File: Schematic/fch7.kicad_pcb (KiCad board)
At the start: 4 copper layers, 39.8 x 41.5 mm, 145 parts, among them IC1 MP9943AGQ-Z, IC2 MP9943AGQ-Z, IC3 STM32H743VIT6, IC4 ICM-42688-P, IC5 MPU-6500, J11 PIN2216, J12 PIN2216, J2 PIN2216, J3 PIN2216, J4 PIN2216, J5 PIN2216, J6 PIN2216, J7 PIN2216, J8 PIN2216, J9 PIN2216, U1 ME6217C33M5G, U10 HDGC1002WR-S-4P, U11 HDGC1002WR-S-4P, U12 E28-2G4M27SX, U15 HDGC1002WR-S-6P, U16 HDGC1002WR-S-8P, U17 HDGC1002WR-S-8P, U2 ME6217C33M5G, U3 LDO-1.8v, U4 QMC5883L, U5 SPL06-001, U6 CSNP1GCR01-BOW, U7 HDGC1002WR-S-6P, U8 HDGC1002WR-S-4P, U9 HDGC1002WR-S-4P, Y1 8MHz

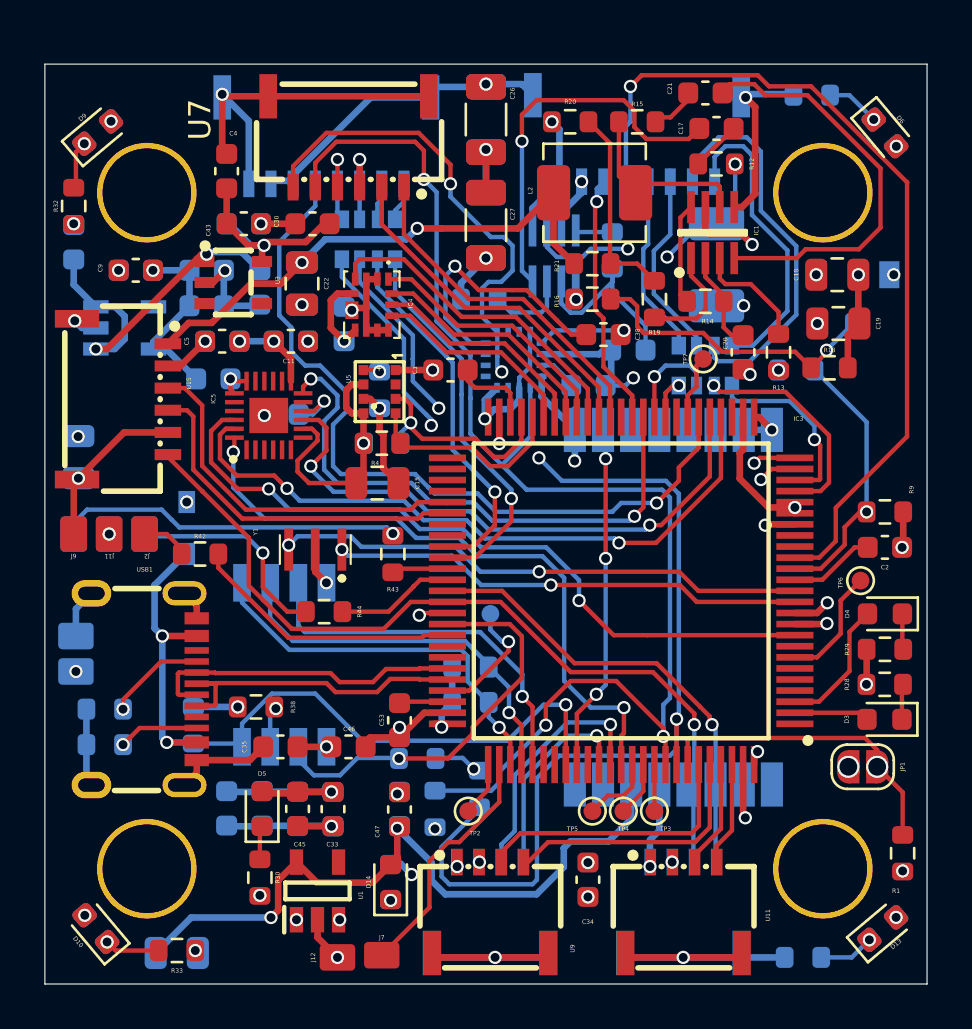
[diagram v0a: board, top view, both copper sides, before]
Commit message: switched mcu package to use TFBGA-100 8x8mm (stm32h743vih6)
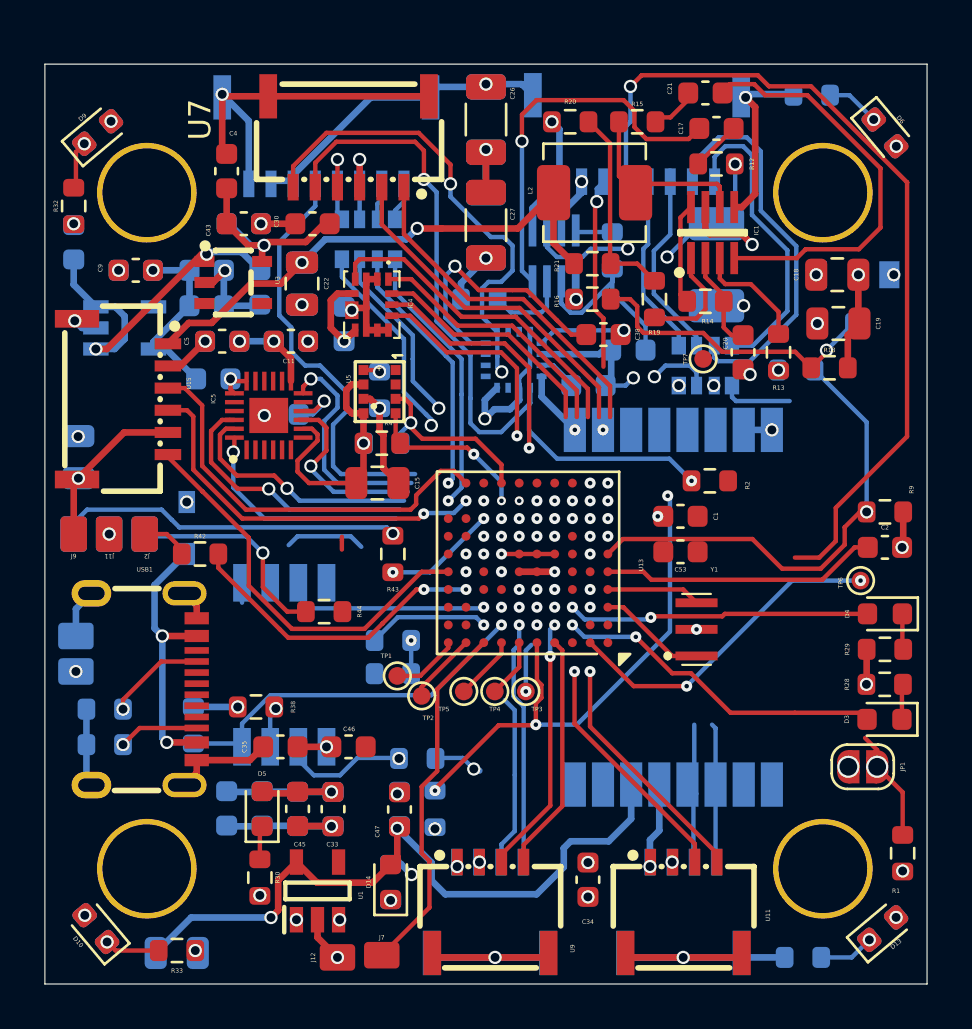
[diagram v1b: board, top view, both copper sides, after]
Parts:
- removed IC3: STM32H743VIT6, fch7:LQFP-100_14x14mm_P0.5mm_STM32H743
- added U13: STM32H742VIHx, Package_BGA:TFBGA-100_8x8mm_Layout10x10_P0.8mm, F.Cu at (86.2, 82.7)
- R2, TP1: moved to F.Cu
- moved Y1 17.6 mm to (93.8, 85.7), turned to -90 degrees
- moved R2 17.4 mm to (94.4, 79.0), turned to 180 degrees
- moved C53 14.8 mm to (93.1, 82.2), turned to 0 degrees
- moved C1 12.3 mm to (93.1, 80.6), turned to 0 degrees
- moved TP3 7.92 mm to (86.1, 88.5)
- moved TP4 7.92 mm to (84.7, 88.5)
- moved TP5 7.92 mm to (83.3, 88.5)
- moved TP2 5.61 mm to (81.4, 88.7)
- moved TP1 5.05 mm to (80.3, 87.8), turned to 0 degrees
- moved R35 3.73 mm to (80.1, 87.7), turned to 0 degrees
- moved R36 3.70 mm to (80.1, 86.2), turned to 0 degrees
- turned C2 to 180 degrees
- turned R4 to 180 degrees
- turned R5 to 180 degrees
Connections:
- C2 pad 1: /MCU/NRST -> GND
- C2 pad 2: GND -> /MCU/NRST
- R2 pad 2: I2C1_SDA -> I2C1_SCL
- R3 pad 2: I2C1_SCL -> I2C1_SDA
- R4 pad 1: VDD_MCU -> I2C2_SCL
- R4 pad 2: I2C2_SCL -> VDD_MCU
- R5 pad 1: VDD_MCU -> I2C2_SDA
- R5 pad 2: I2C2_SDA -> VDD_MCU
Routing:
- net I2C1_SCL: track 61.4 -> 33.3 mm
- net SPI1_IMU1_CS: track 32.8 -> 12.1 mm, vias 2 -> 1
- net SPI1_MOSI: track 29.4 -> 10.2 mm
- net SPI1_SCLK: track 30.0 -> 10.9 mm
- net SPI1_MISO: track 26.4 -> 8.35 mm
- net GND: track 151.8 -> 134.3 mm, vias 44 -> 42
- net SDIO_D2: track 17.8 -> 0.90 mm, vias 1 -> 0
- net /MCU/PH1-OSC_OUT: track 24.4 -> 7.89 mm, vias 2 -> 0
- net /MCU/PH0-OSC_IN: track 22.0 -> 5.49 mm, vias 2 -> 0
- net SENS_CUR2: track 35.9 -> 19.4 mm, vias 1 -> 0
- net NRESET_RECV: track 15.7 -> 0.17 mm, vias 3 -> 2
- net IMU2_SPI1_EXTI1: track 25.6 -> 10.1 mm
- net PWM_5: track 27.6 -> 12.9 mm
- net UART6_TX: track 21.1 -> 6.47 mm, vias 1 -> 0
- net /MCU/OTG_FS-: track 14.4 -> 0.00 mm
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
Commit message: minor update on routing
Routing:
- net SENS_CUR2: track 19.4 -> 26.7 mm, vias 0 -> 2
- net UART1_RX: track 15.7 -> 8.71 mm
- net PWM_2: track 2.83 -> 9.75 mm
- net UART1_TX: track 15.9 -> 9.45 mm
- net IMU1_SPI4_EXTI2: track 15.0 -> 19.8 mm, vias 1 -> 2
- net SPI4_MISO: track 11.8 -> 15.6 mm, vias 1 -> 2
- net UART3_TX: track 18.5 -> 14.7 mm
- net SPI4_MOSI: track 10.8 -> 13.8 mm

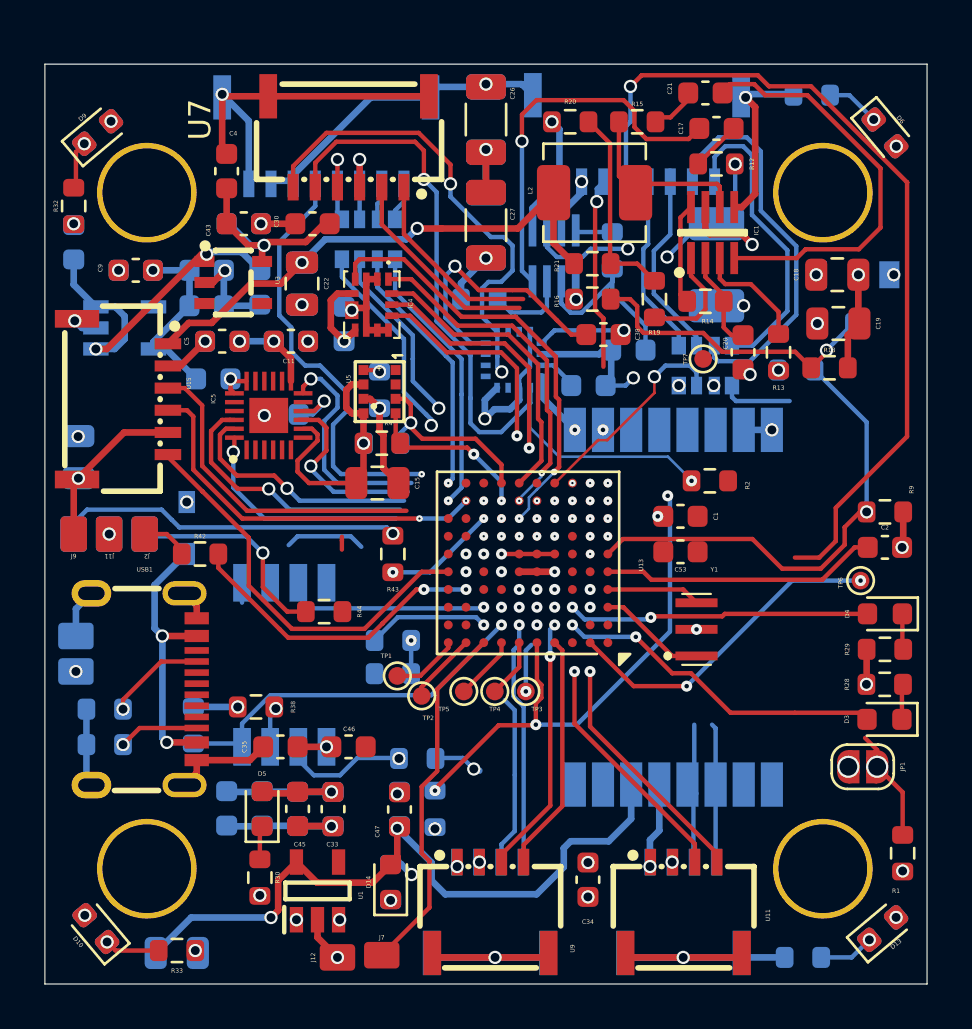
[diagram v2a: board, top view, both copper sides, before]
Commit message: update routing and constraints according to jlcpcb specs
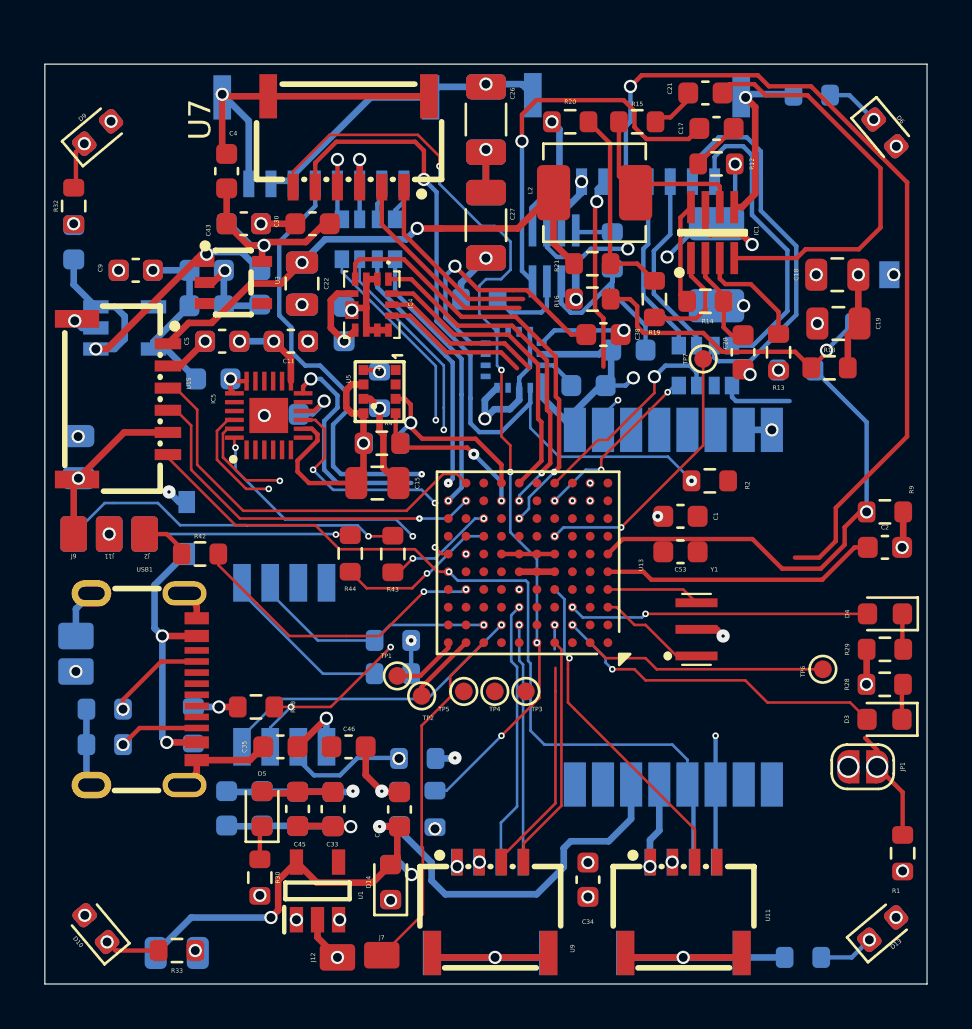
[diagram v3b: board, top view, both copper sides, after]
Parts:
- removed H1: MountingHole, fch7:MountingHole_quad_30.5x30.5
- moved TP6 4.35 mm to (99.5, 87.5)
- moved R44 2.88 mm to (78.2, 82.3), turned to -90 degrees
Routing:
- net UART6_TX: track 6.47 -> 24.0 mm, vias 0 -> 2
- net I2C1_SDA: track 56.2 -> 43.5 mm
- net AIRS: track 0.00 -> 12.3 mm, vias 1 -> 2
- net UART6_RX: track 25.7 -> 37.6 mm, vias 0 -> 1
- net UART8_TX: track 11.0 -> 0.00 mm, vias 2 -> 0
- net GND: track 134.3 -> 144.0 mm, vias 42 -> 37
- net SDIO_CLK: track 9.79 -> 1.16 mm, vias 1 -> 0
- net SPI1_MOSI: track 10.2 -> 18.4 mm, vias 2 -> 3
- net PWM_1: track 0.40 -> 8.05 mm, vias 2 -> 3
- net SPI1_MISO: track 8.35 -> 15.8 mm, vias 2 -> 3
- net PWM_10: track 0.00 -> 7.30 mm
- net SDIO_D2: track 0.90 -> 7.94 mm
- net SPI1_SCLK: track 10.9 -> 4.69 mm, vias 2 -> 1
- net PWM_5: track 12.9 -> 18.6 mm
- net SDIO_D3: track 6.12 -> 11.3 mm
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
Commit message: update on routing
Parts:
- moved R1 11.3 mm to (99.5, 85.1)
- moved TP6 10.1 mm to (89.5, 88.7)
- moved JP1 7.80 mm to (97.4, 85.2), turned to 90 degrees
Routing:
- net GND: track 144.0 -> 174.9 mm, vias 37 -> 39
- net NRESET_RECV: track 1.62 -> 18.5 mm, vias 1 -> 2
- net UART8_TX: track 0.00 -> 15.3 mm, vias 0 -> 2
- net /MCU/OTG_FS-: track 0.00 -> 15.1 mm
- net /MCU/OTG_FS+: track 0.05 -> 14.8 mm
- net SPI1_SCLK: track 4.69 -> 18.7 mm, vias 1 -> 2
- net SDIO_D1: track 6.19 -> 17.2 mm, vias 1 -> 2
- net UART1_TX: track 9.45 -> 20.1 mm, vias 0 -> 2
- net PWM_3: track 0.00 -> 10.4 mm, vias 0 -> 3
- net I2C1_SCL: track 33.2 -> 43.5 mm, vias 2 -> 3
- net SDIO_CLK: track 1.16 -> 10.2 mm, vias 0 -> 1
- net /MCU/BOOT0: track 5.08 -> 13.9 mm, vias 1 -> 3
- net VDD_MCU: track 50.1 -> 58.7 mm, vias 13 -> 15
- net UART1_RX: track 8.71 -> 17.2 mm
- net /MCU/VCAP2: track 0.00 -> 8.48 mm, vias 0 -> 3
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
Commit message: update routing
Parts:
- moved C40 0.10 mm to (78.0, 71.9)
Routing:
- net GND: track 174.9 -> 193.1 mm, vias 39 -> 38
- net 5V: track 20.2 -> 36.3 mm, vias 16 -> 15
- net VDD_MCU: track 58.7 -> 65.1 mm, vias 15 -> 17
- net /Power/LC_5V: track 12.5 -> 6.67 mm, vias 3 -> 2
- net VCC_ICM: track 14.1 -> 17.1 mm
- net VBAT: track 24.5 -> 26.9 mm
- net SDIO_CMD: track 14.2 -> 16.1 mm
- net Net-(D14-K): track 0.21 -> 1.96 mm
- net Net-(D10-K): track 2.49 -> 3.75 mm
- net Net-(U4-SETP): track 11.6 -> 11.0 mm
- net Net-(D8-K): track 2.14 -> 2.75 mm

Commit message: update routing
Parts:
- C1, C10, C11, C12, C14, C16, C17, C2, C20, C21, C28, C29, C3, C30, C31, C32, C33, C34, C35, C36, C37, C38, C39, C4, C40, C41, C43, C45, C46, C47, C5, C50, C53, C6, C7, C8, C9: footprint Capacitor_SMD:C_0603_1608Metric -> Capacitor_SMD:C_0402_1005Metric
- C13, C15, C18, C19, C22, C23, C48: footprint Capacitor_SMD:C_0805_2012Metric -> Capacitor_SMD:C_0402_1005Metric
- C24, C25, C26, C27: footprint Capacitor_SMD:C_1206_3216Metric -> Capacitor_SMD:C_0603_1608Metric
- R1, R10, R11, R12, R13, R14, R15, R16, R17, R18, R19, R2, R20, R21, R22, R28, R29, R3, R30, R31, R32, R33, R34, R35, R36, R37, R38, R39, R4, R40, R42, R43, R44, R5, R6, R7, R8, R9: footprint Resistor_SMD:R_0603_1608Metric -> Capacitor_SMD:C_0402_1005Metric
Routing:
- net GND: track 193.1 -> 207.8 mm, vias 38 -> 30
- net 5V: track 36.3 -> 43.5 mm, vias 15 -> 11
- net /Power/LC_5V: track 6.67 -> 12.6 mm, vias 2 -> 3
- net VDD_MCU: track 65.1 -> 71.0 mm
- net VBAT: track 26.9 -> 32.5 mm, vias 5 -> 4
- net Net-(D12-K): track 2.59 -> 3.92 mm, vias 1 -> 0
- net PWM_1: track 8.05 -> 9.23 mm
- net UART6_TX: track 24.3 -> 25.4 mm
- net Net-(D6-K): track 2.47 -> 3.56 mm
- net /Power/FB_5V: track 0.52 -> 1.58 mm
- net PWM_3: track 10.4 -> 11.0 mm
- net PWM_2: track 8.95 -> 9.48 mm
- net VDD_RECV: vias 2 -> 1
- net VCC_ICM: vias 2 -> 1

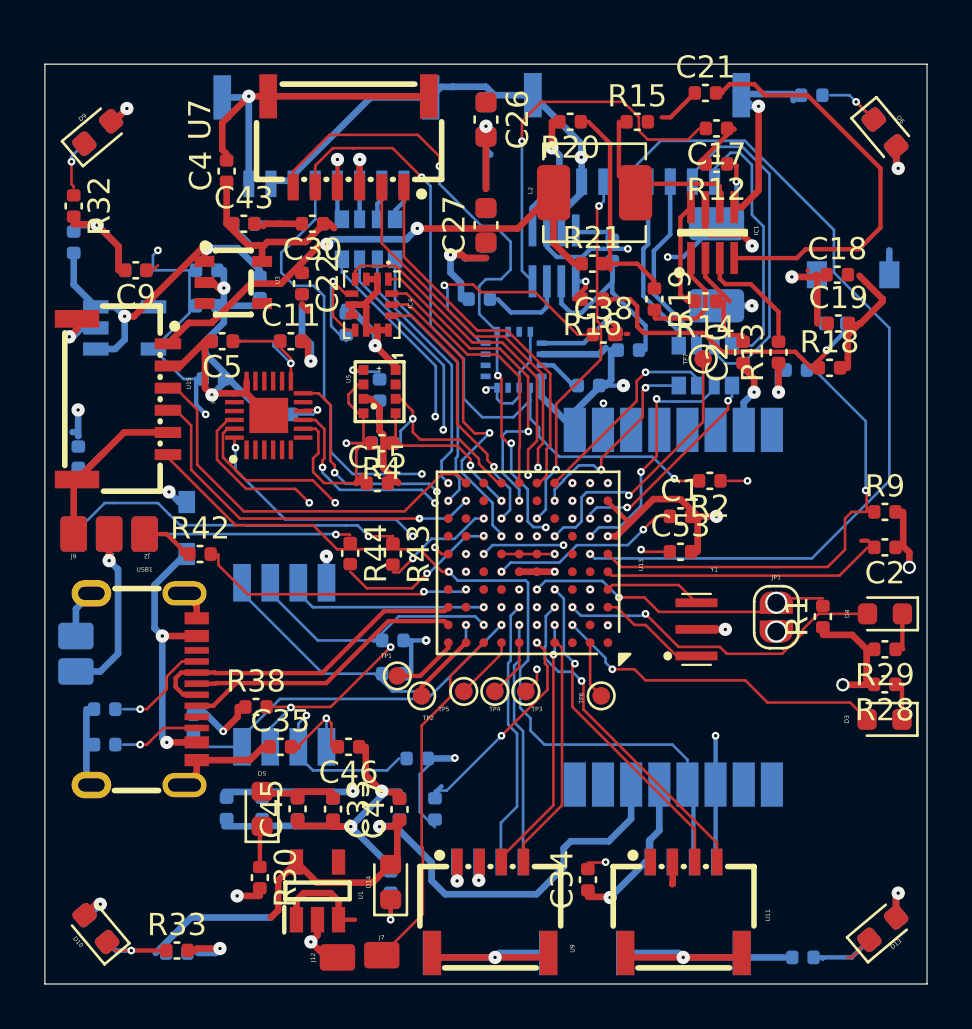
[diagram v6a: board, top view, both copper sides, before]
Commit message: fix: update fch7 library path and description in fp-lib-table
- Changed the URI for the fch7 library to use the KIPRJMOD variable for better project portability.
- Updated the description to specify that it contains footprints for fch7.
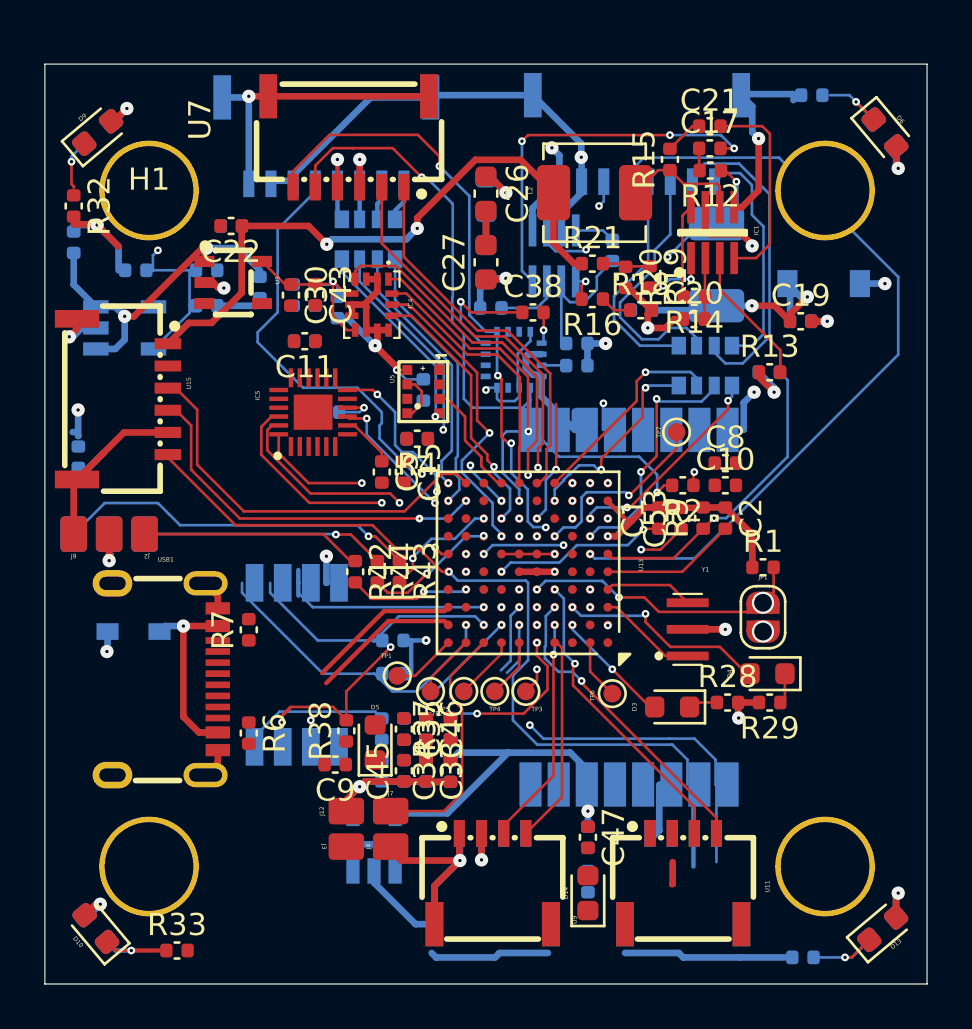
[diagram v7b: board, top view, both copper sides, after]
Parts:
- added H1: MountingHole, fch7:MountingHole_quad_30.5x30.5, F.Cu at (69.1, 65.9)
- C10, C8, J3, J4, R37, R6, R7: moved to F.Cu
- C18, C4, R30, U1: moved to B.Cu
- moved C9 24.0 mm to (77.5, 91.8)
- moved C10 23.6 mm to (95.1, 79.2)
- moved C8 23.4 mm to (95.1, 78.2), turned to 0 degrees
- moved J4 17.1 mm to (80.0, 95.5), turned to 180 degrees
- moved C48 14.8 mm to (82.7, 92.1), turned to -90 degrees
- moved J3 14.5 mm to (78.0, 95.5), turned to 0 degrees
- moved D3 9.60 mm to (92.7, 89.2)
- moved C5 9.31 mm to (79.6, 78.6), turned to -90 degrees
- moved D14 8.91 mm to (88.9, 97.6)
- moved R18 8.91 mm to (91.3, 71.3)
- moved R40 8.90 mm to (88.9, 97.1)
- moved R17 8.78 mm to (91.3, 71.3), turned to 180 degrees
- moved C37 8.76 mm to (80.6, 90.2), turned to -90 degrees
- moved C50 8.60 mm to (88.9, 95.1), turned to -90 degrees
- moved C47 8.59 mm to (88.9, 95.1), turned to -90 degrees
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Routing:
- net GND: track 207.8 -> 137.8 mm, vias 30 -> 20
- net VDD_MCU: track 71.0 -> 29.4 mm, vias 17 -> 9
- net VDD_RECV: track 33.2 -> 15.4 mm
- net Net-(R16-Pad1): track 13.9 -> 1.23 mm, vias 1 -> 0
- net LED_0: track 15.2 -> 5.36 mm
- net UART7_RX: track 16.6 -> 6.84 mm
- net Net-(IC1-BST): track 19.5 -> 9.97 mm
- net UART2_RX: track 12.2 -> 3.19 mm
- net UART2_TX: track 11.0 -> 2.39 mm
- net /MCU/OTG_FS-: track 15.1 -> 6.93 mm
- net /MCU/OTG_FS+: track 14.8 -> 6.79 mm
- net Net-(J2-Pin_1): track 2.18 -> 10.0 mm
- net VCC_ICM: track 17.1 -> 9.36 mm
- net SENS_VOL: track 21.5 -> 14.0 mm
- net Net-(R19-Pad1): track 9.43 -> 2.19 mm
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- removed copper zone on In2.Cu, net 5V5_BEC
